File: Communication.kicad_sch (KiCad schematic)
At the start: 50 parts, among them J2 USB_A_Stacked, J3 USB_A_Stacked, U4 X1000, U6 FE2.1, Y1 12MHz

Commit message: Update (Display)
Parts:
- removed D11, D3, D5, D7, D9: LED, symbol Device:LED
- removed unit 5 of U4
- removed Y1: 12MHz, symbol Device:Crystal_GND24_Small
- added C55: 100n, Capacitor_SMD:C_0402_1005Metric, symbol Device:C
- added Y1: 12MHz, Crystal:Crystal_SMD_ECS_CSM3X-2Pin_7.6x4.1mm, symbol Device:Crystal
- C47, C48: value C -> 20p; LCSC (none) -> C880615
- D10, D12, D13, D4, D6, D8: footprint (none) -> LED_SMD:LED_0402_1005Metric; LCSC (none) -> C965795
- R14: value R -> 100K; footprint (none) -> Resistor_SMD:R_0402_1005Metric
- R15: value R -> 1MEG; LCSC (none) -> C2909328
- R17, R18, R19, R20, R21, R22, R23, R24: value R -> 1K; footprint (none) -> Resistor_SMD:R_0402_1005Metric
- U4: footprint (none) -> TheBrutzlers_Lib:BGA256C80P16X16_1300X1300X130N
- renumbered C55 to C56, C56 to C57, C57 to C58, C58 to C59, C59 to C60, C60 to C61, C61 to C62
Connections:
- net DRV: now also R24.1; no longer R24.2
- net GND: now also C55.1
- net at C44.1, C45.1, C46.1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: now also R14.1; no longer R15.1
- net at U6.40 (XRST): now also R14.2, C55.2; no longer R15.2
- net at C47.2, U6.23 (CLK_OUT): now also R15.1, Y1.2; no longer R14.1
- net at C48.2, U6.22 (CLKIN): now also R15.2, Y1.1; no longer R14.2
- net at D13.2 (A): now also R24.2; no longer R24.1

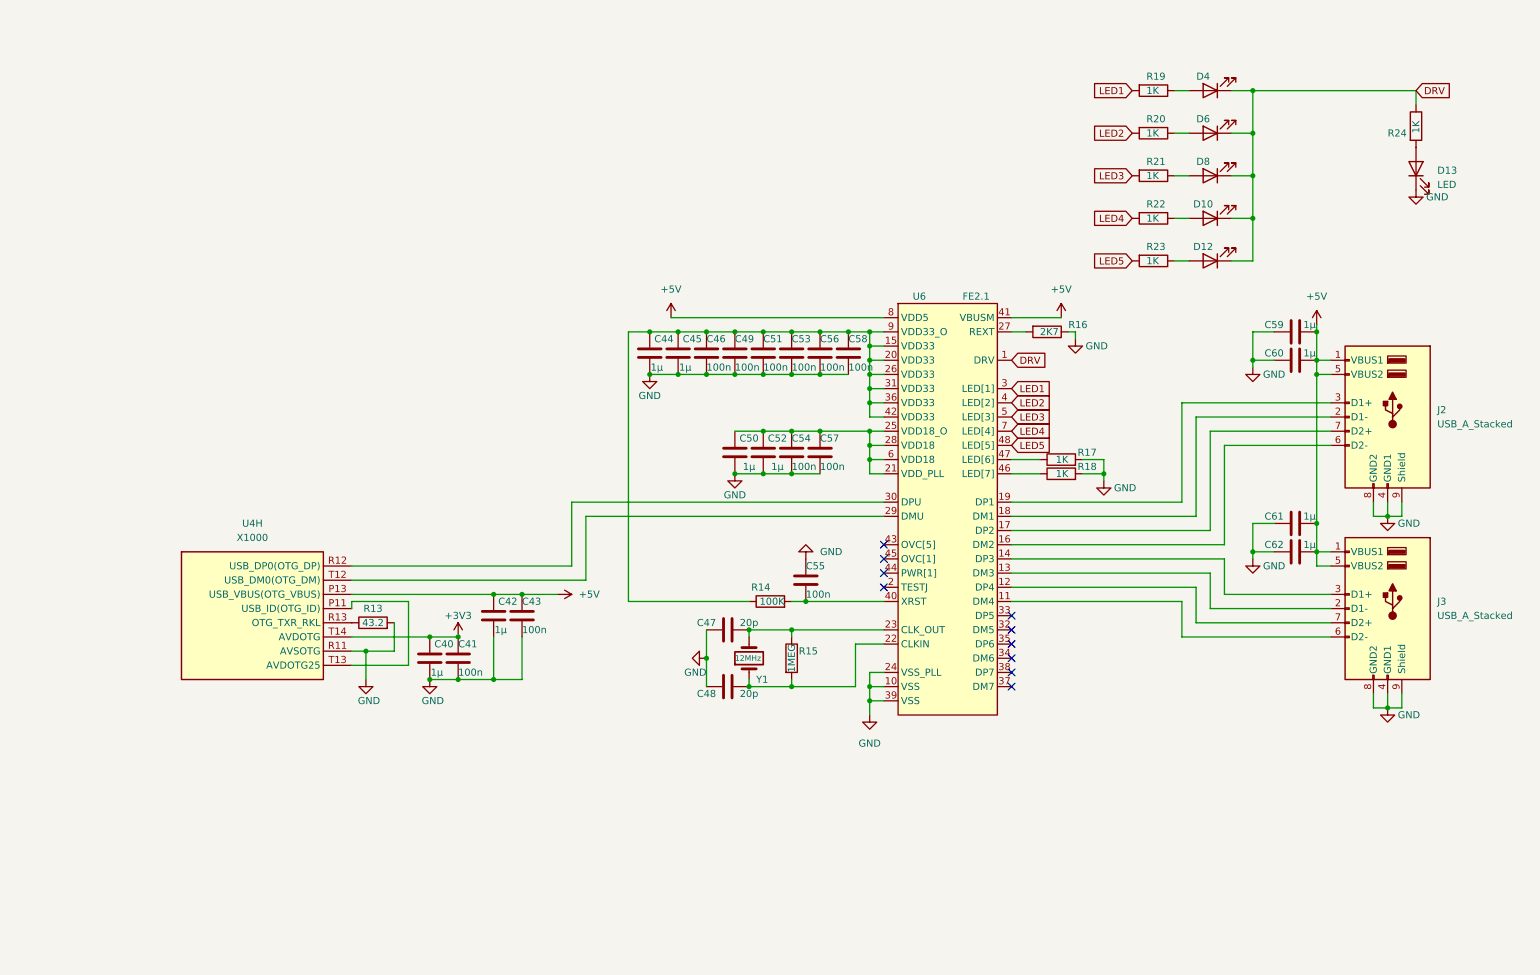
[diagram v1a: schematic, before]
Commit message: Add Audio
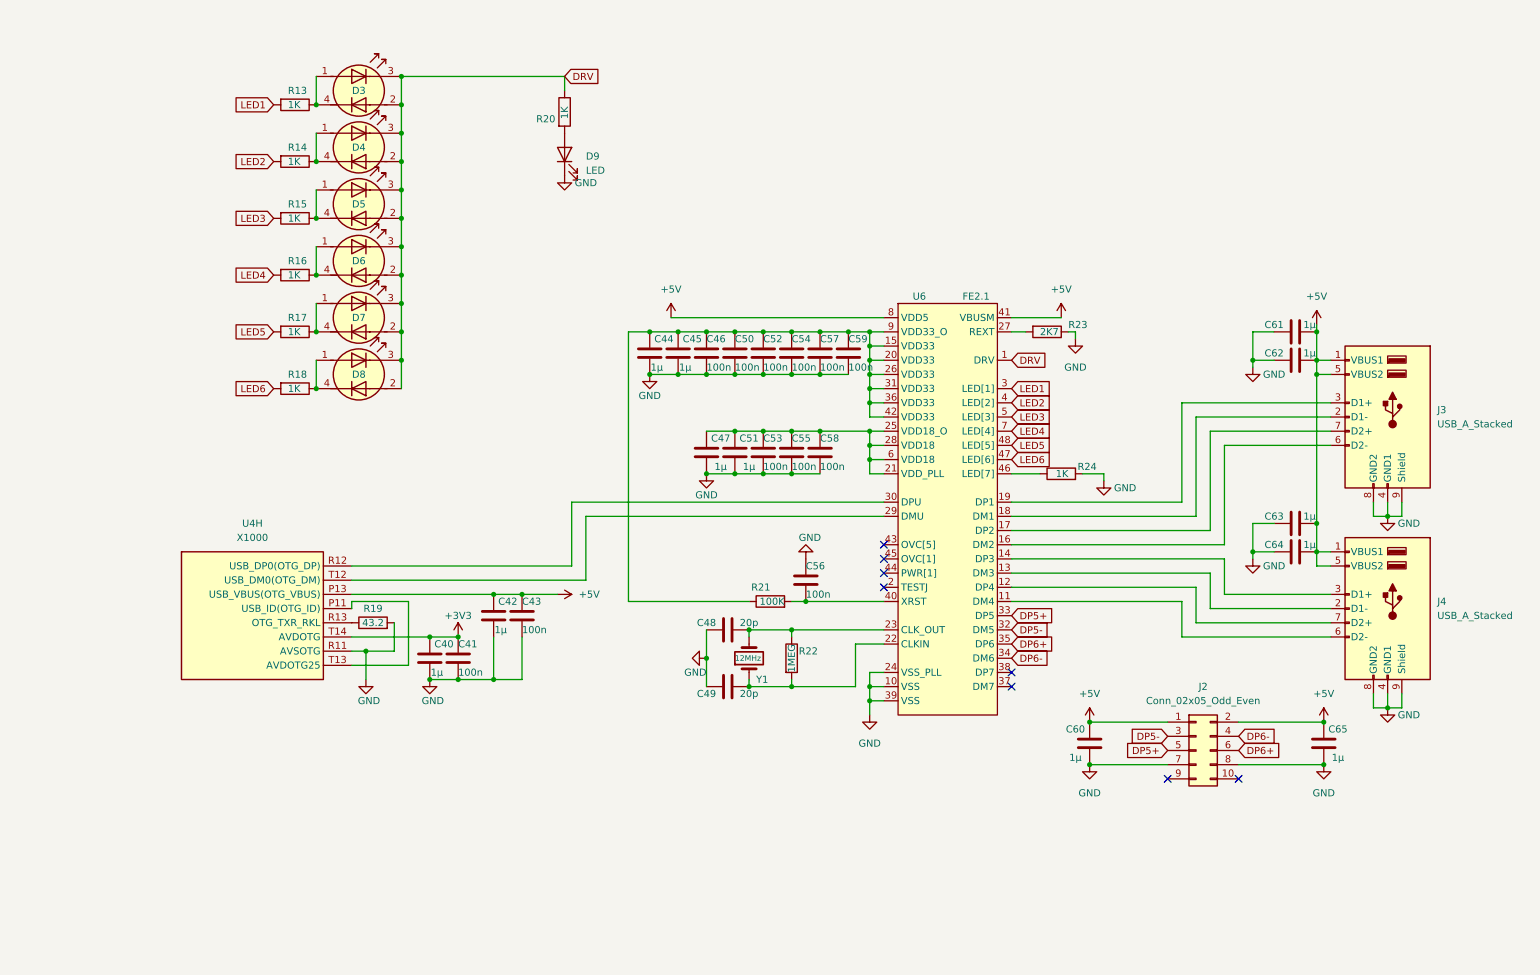
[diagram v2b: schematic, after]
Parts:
- removed D10, D12, D4, D6, D8: LED, LED_SMD:LED_0402_1005Metric, symbol Device:LED
- removed R17: 1K, Resistor_SMD:R_0402_1005Metric, symbol Device:R
- added C58: 100n, Capacitor_SMD:C_0402_1005Metric, symbol Device:C
- added C60, C65: 1µ, Capacitor_SMD:C_0402_1005Metric, symbol Device:C
- added D3, D4, D5, D6, D7, D8: LED_Dual_LED, TheBrutzlers_Lib:DUAL_LED_0603, symbol TheBrutzlers_Lib:LED_Dual_LED
- added J2: Conn_02x05_Odd_Even, Connector_PinHeader_2.54mm:PinHeader_2x05_P2.54mm_Vertical, symbol Connector_Generic:Conn_02x05_Odd_Even
- added R18: 1K, Resistor_SMD:R_0402_1005Metric, symbol Device:R
- R22: renamed from R15; footprint (none) -> Resistor_SMD:R_0402_1005Metric
- renumbered C50 to C47, C47 to C48, C48 to C49, C49 to C50, C52 to C51, C51 to C52, C54 to C53, C53 to C54, C57 to C55, C55 to C56, C56 to C57, C58 to C59, C59 to C61, C60 to C62, C61 to C63, C62 to C64, D13 to D9, J2 to J3, J3 to J4, R19 to R13, R20 to R14, R21 to R15, R22 to R16, R23 to R17, R13 to R19, R24 to R20, R14 to R21, R16 to R23, R18 to R24
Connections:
- net +5V: now also C60.1, C65.1, J2.1 (Pin_1), J2.2 (Pin_2)
- net DRV: now also D3.2 (A2), D3.3 (K1), D4.2 (A2), D4.3 (K1), D5.2 (A2), D5.3 (K1), D6.2 (A2), D6.3 (K1), D7.2 (A2), D7.3 (K1), D8.2 (A2), D8.3 (K1)
- net GND: now also C58.2, C60.2, C65.2, J2.7 (Pin_7), J2.8 (Pin_8)
- net at C47.1, C51.1, C53.1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: now also C58.1
- net at R16.1: now also D6.1 (A1), D6.4 (K2)
- net at R14.1: now also D4.1 (A1), D4.4 (K2)
- net at R15.1: now also D5.1 (A1), D5.4 (K2)
- net LED6: now reaches U6.47 (LED[6])
- net LED6: now also R18.2
- net at R13.1: now also D3.1 (A1), D3.4 (K2)
- net at R17.1: now also D7.1 (A1), D7.4 (K2)
- net DP5-: now reaches U6.32 (DM5)
- net DP5-: now also J2.3 (Pin_3)
- net DP5+: now reaches U6.33 (DP5)
- net DP5+: now also J2.5 (Pin_5)
- net DP6-: now reaches U6.34 (DM6)
- net DP6-: now also J2.4 (Pin_4)
- net DP6+: now reaches U6.35 (DP6)
- net DP6+: now also J2.6 (Pin_6)
- new net: D8.1 (A1), D8.4 (K2), R18.1
- no-connect marks 10 -> 8
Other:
- moved on the sheet: C47, C51, C53, C55, D9, R13, R14, R15, R16, R17, R20

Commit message: New i.mx6 Version
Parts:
- added U? (x2): IMX6UL, TheBrutzlers_Lib:IMX6UL_BGA289, symbol TheBrutzlers_Lib:IMX6UL
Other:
- moved on the sheet: D3, D4, D5, D6, D7, D8, D9, R13, R14, R15, R16, R17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
